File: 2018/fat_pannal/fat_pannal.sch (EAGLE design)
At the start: 31 parts, among them IC1 MEGA8-P, Q2 BUZ11BV, Q3 BUZ11BV, Q4 BUZ11BV, Q5 BUZ11BV, U1 TSR_1-2450

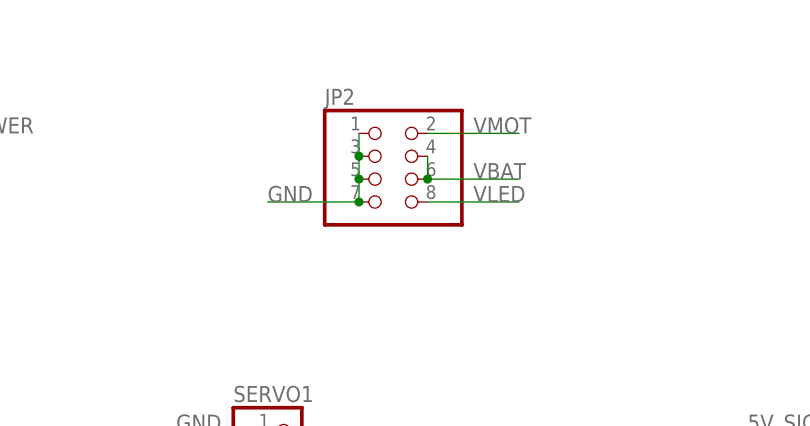
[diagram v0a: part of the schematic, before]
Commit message: [FAT pannal] Split cavalier in two.
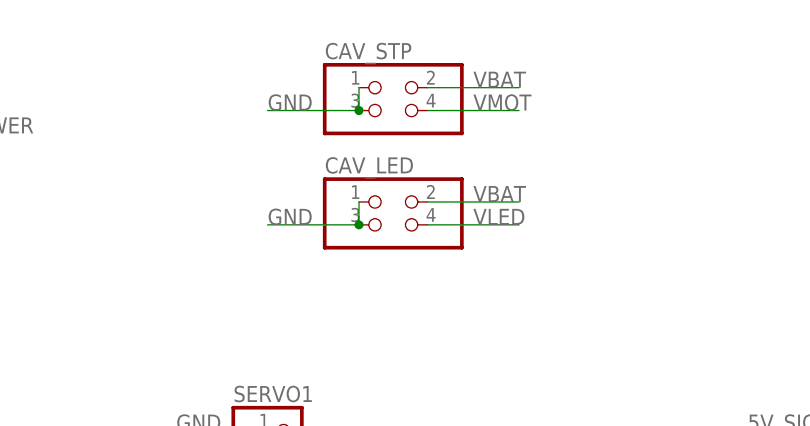
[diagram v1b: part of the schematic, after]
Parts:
- removed JP2: (no value), pinhead:PINHD-2X4
- added CAV_LED, CAV_STP: (no value), pinhead:PINHD-2X2
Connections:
- net GND: now also CAV_LED.1, CAV_LED.3, CAV_STP.1, CAV_STP.3; no longer JP2.1, JP2.3, JP2.5, JP2.7
- net VBAT: now also CAV_LED.2, CAV_STP.2; no longer JP2.4, JP2.6
- net VLED: now also CAV_LED.4; no longer JP2.8
- net VMOT: now also CAV_STP.4; no longer JP2.2
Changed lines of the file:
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@@
 <part name="SERVO3" library="pinhead" deviceset="PINHD-1X3" device=""/>
 <part name="REGU_5V_POWER" library="diy-modules" deviceset="DC-DC-STEP-DOWN-LM2596" device=""/>
-<part name="JP2" library="pinhead" deviceset="PINHD-2X4" device=""/>
 <part name="I2C" library="pinhead" deviceset="PINHD-1X4" device=""/>
 <part name="UART" library="pinhead" deviceset="PINHD-1X4" device=""/>
 <part name="X1" library="con-ptr500" deviceset="AK300/2" device=""/>
 <part name="U1" library="_traco_tsr-1" deviceset="TSR_1-*" device="" technology="2450"/>
+<part name="CAV_STP" library="pinhead" deviceset="PINHD-2X2" device=""/>
+<part name="CAV_LED" library="pinhead" deviceset="PINHD-2X2" device=""/>
 </parts>
 <sheets>
@@
 <instance part="SERVO3" gate="A" x="114.3" y="78.74"/>
 <instance part="REGU_5V_POWER" gate="G$1" x="53.34" y="134.62"/>
-<instance part="JP2" gate="A" x="124.46" y="134.62"/>
 <instance part="I2C" gate="A" x="180.34" y="83.82"/>
 <instance part="UART" gate="A" x="180.34" y="101.6"/>
@@
 <instance part="X1" gate="-2" x="5.08" y="134.62"/>
 <instance part="U1" gate="G$1" x="20.32" y="111.76"/>
+<instance part="CAV_STP" gate="A" x="127" y="142.24"/>
+<instance part="CAV_LED" gate="A" x="127" y="129.54"/>
 </instances>
 <busses>
@@
 </segment>
 <segment>
-<pinref part="JP2" gate="A" pin="1"/>
-<pinref part="JP2" gate="A" pin="3"/>
-<wire x1="121.92" y1="139.7" x2="121.92" y2="137.16" width="0.1524" layer="91"/>
-<pinref part="JP2" gate="A" pin="5"/>
-<wire x1="121.92" y1="137.16" x2="121.92" y2="134.62" width="0.1524" layer="91"/>
-<junction x="121.92" y="137.16"/>
-<pinref part="JP2" gate="A" pin="7"/>
-<wire x1="121.92" y1="134.62" x2="121.92" y2="132.08" width="0.1524" layer="91"/>
-<junction x="121.92" y="134.62"/>
-<wire x1="121.92" y1="132.08" x2="111.76" y2="132.08" width="0.1524" layer="91"/>
-<junction x="121.92" y="132.08"/>
-<label x="111.76" y="132.08" size="1.778" layer="95"/>
-</segment>
-<segment>
 <pinref part="STEPPER_DRIVER" gate="G$1" pin="GND2"/>
 <wire x1="114.3" y1="48.26" x2="121.92" y2="48.26" width="0.1524" layer="91"/>
@@
 <wire x1="20.32" y1="101.6" x2="25.4" y2="101.6" width="0.1524" layer="91"/>
 <label x="22.86" y="101.6" size="1.778" layer="95"/>
+</segment>
+<segment>
+<pinref part="CAV_LED" gate="A" pin="1"/>
+<pinref part="CAV_LED" gate="A" pin="3"/>
+<wire x1="121.92" y1="132.08" x2="121.92" y2="129.54" width="0.1524" layer="91"/>
+<wire x1="121.92" y1="129.54" x2="111.76" y2="129.54" width="0.1524" layer="91"/>
+<junction x="121.92" y="129.54"/>
+<label x="111.76" y="129.54" size="1.778" layer="95"/>
+</segment>
+<segment>
+<pinref part="CAV_STP" gate="A" pin="3"/>
+<wire x1="111.76" y1="142.24" x2="121.92" y2="142.24" width="0.1524" layer="91"/>
+<pinref part="CAV_STP" gate="A" pin="1"/>
+<wire x1="121.92" y1="142.24" x2="121.92" y2="144.78" width="0.1524" layer="91"/>
+<junction x="121.92" y="142.24"/>
+<label x="111.76" y="142.24" size="1.778" layer="95"/>
 </segment>
 </net>
@@
 </segment>
 <segment>
-<pinref part="JP2" gate="A" pin="8"/>
-<wire x1="129.54" y1="132.08" x2="139.7" y2="132.08" width="0.1524" layer="91"/>
-<label x="134.62" y="132.08" size="1.778" layer="95"/>
+<pinref part="CAV_LED" gate="A" pin="4"/>
+<wire x1="129.54" y1="129.54" x2="139.7" y2="129.54" width="0.1524" layer="91"/>
+<label x="134.62" y="129.54" size="1.778" layer="95"/>
 </segment>
 </net>
@@
 </segment>
 <segment>
-<pinref part="JP2" gate="A" pin="4"/>
-<pinref part="JP2" gate="A" pin="6"/>
-<wire x1="129.54" y1="137.16" x2="129.54" y2="134.62" width="0.1524" layer="91"/>
-<wire x1="129.54" y1="134.62" x2="139.7" y2="134.62" width="0.1524" layer="91"/>
-<junction x="129.54" y="134.62"/>
-<label x="134.62" y="134.62" size="1.778" layer="95"/>
-</segment>
-<segment>
 <pinref part="U1" gate="G$1" pin="VI"/>
 <wire x1="10.16" y1="111.76" x2="5.08" y2="111.76" width="0.1524" layer="91"/>
 <label x="2.54" y="111.76" size="1.778" layer="95"/>
 </segment>
+<segment>
+<pinref part="CAV_LED" gate="A" pin="2"/>
+<wire x1="129.54" y1="132.08" x2="139.7" y2="132.08" width="0.1524" layer="91"/>
+<label x="134.62" y="132.08" size="1.778" layer="95"/>
+</segment>
+<segment>
+<pinref part="CAV_STP" gate="A" pin="2"/>
+<wire x1="139.7" y1="144.78" x2="129.54" y2="144.78" width="0.1524" layer="91"/>
+<label x="134.62" y="144.78" size="1.778" layer="95"/>
+</segment>
 </net>
 <net name="VMOT" class="0">
-<segment>
-<pinref part="JP2" gate="A" pin="2"/>
-<wire x1="129.54" y1="139.7" x2="139.7" y2="139.7" width="0.1524" layer="91"/>
-<label x="134.62" y="139.7" size="1.778" layer="95"/>
-</segment>
 <segment>
 <pinref part="STEPPER_DRIVER" gate="G$1" pin="VMOT"/>
@@
 <label x="119.38" y="50.8" size="1.778" layer="95"/>
 </segment>
-</net>
+<segment>
+<pinref part="CAV_STP" gate="A" pin="4"/>
+<wire x1="129.54" y1="142.24" x2="139.7" y2="142.24" width="0.1524" layer="91"/>
+<label x="134.62" y="142.24" size="1.778" layer="95"/>
+</segment>
+</net>

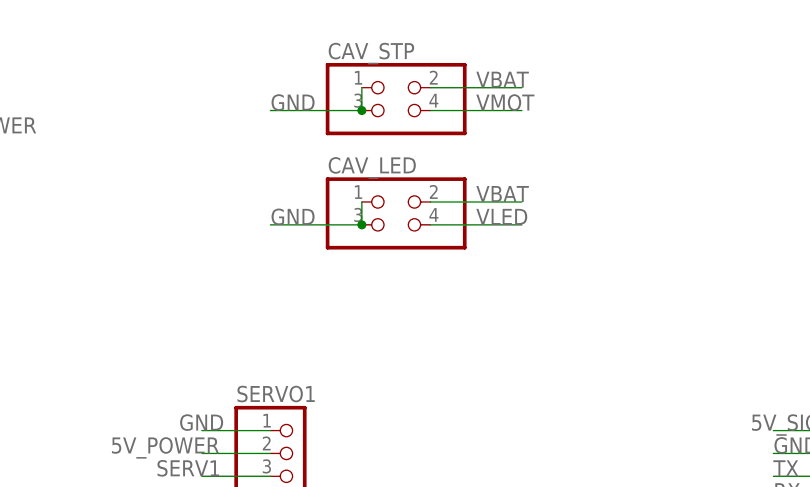
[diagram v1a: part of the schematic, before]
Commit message: [FAT pannal] Begins routing.
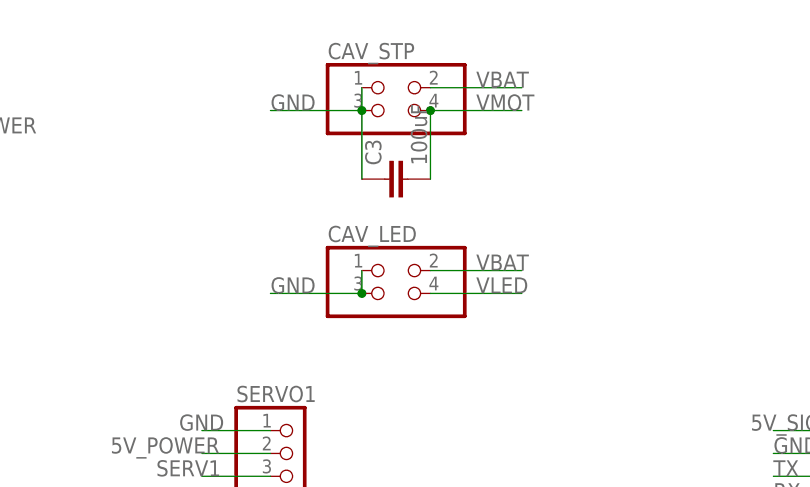
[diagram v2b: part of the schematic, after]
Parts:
- added C3: 100uF, rcl:C-EU025-050X050
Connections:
- net GND: now also C3.1
- net VMOT: now also C3.2
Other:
- moved on the sheet: CAV_LED
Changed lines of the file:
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@@
 <part name="CAV_STP" library="pinhead" deviceset="PINHD-2X2" device=""/>
 <part name="CAV_LED" library="pinhead" deviceset="PINHD-2X2" device=""/>
+<part name="C3" library="rcl" deviceset="C-EU" device="025-050X050" value="100uF"/>
 </parts>
 <sheets>
@@
 <instance part="U1" gate="G$1" x="20.32" y="111.76"/>
 <instance part="CAV_STP" gate="A" x="127" y="142.24"/>
-<instance part="CAV_LED" gate="A" x="127" y="129.54"/>
+<instance part="CAV_LED" gate="A" x="127" y="121.92"/>
+<instance part="C3" gate="G$1" x="124.46" y="134.62" rot="R90"/>
 </instances>
 <busses>
@@
 <pinref part="CAV_LED" gate="A" pin="1"/>
 <pinref part="CAV_LED" gate="A" pin="3"/>
-<wire x1="121.92" y1="132.08" x2="121.92" y2="129.54" width="0.1524" layer="91"/>
-<wire x1="121.92" y1="129.54" x2="111.76" y2="129.54" width="0.1524" layer="91"/>
-<junction x="121.92" y="129.54"/>
-<label x="111.76" y="129.54" size="1.778" layer="95"/>
+<wire x1="121.92" y1="124.46" x2="121.92" y2="121.92" width="0.1524" layer="91"/>
+<wire x1="121.92" y1="121.92" x2="111.76" y2="121.92" width="0.1524" layer="91"/>
+<junction x="121.92" y="121.92"/>
+<label x="111.76" y="121.92" size="1.778" layer="95"/>
 </segment>
 <segment>
@@
 <junction x="121.92" y="142.24"/>
 <label x="111.76" y="142.24" size="1.778" layer="95"/>
+<pinref part="C3" gate="G$1" pin="1"/>
+<wire x1="121.92" y1="134.62" x2="121.92" y2="142.24" width="0.1524" layer="91"/>
 </segment>
 </net>
@@
 <segment>
 <pinref part="CAV_LED" gate="A" pin="4"/>
-<wire x1="129.54" y1="129.54" x2="139.7" y2="129.54" width="0.1524" layer="91"/>
-<label x="134.62" y="129.54" size="1.778" layer="95"/>
+<wire x1="129.54" y1="121.92" x2="139.7" y2="121.92" width="0.1524" layer="91"/>
+<label x="134.62" y="121.92" size="1.778" layer="95"/>
 </segment>
 </net>
@@
 <segment>
 <pinref part="CAV_LED" gate="A" pin="2"/>
-<wire x1="129.54" y1="132.08" x2="139.7" y2="132.08" width="0.1524" layer="91"/>
-<label x="134.62" y="132.08" size="1.778" layer="95"/>
+<wire x1="129.54" y1="124.46" x2="139.7" y2="124.46" width="0.1524" layer="91"/>
+<label x="134.62" y="124.46" size="1.778" layer="95"/>
 </segment>
 <segment>
@@
 <wire x1="129.54" y1="142.24" x2="139.7" y2="142.24" width="0.1524" layer="91"/>
 <label x="134.62" y="142.24" size="1.778" layer="95"/>
-</segment>
-</net>
+<pinref part="C3" gate="G$1" pin="2"/>
+<wire x1="129.54" y1="134.62" x2="129.54" y2="142.24" width="0.1524" layer="91"/>
+<junction x="129.54" y="142.24"/>
+</segment>
+</net>

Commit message: [FAT pannal] Finish board V1.
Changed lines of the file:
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@@
 <pinref part="STEPPER_DRIVER" gate="G$1" pin="GND"/>
 <wire x1="114.3" y1="33.02" x2="124.46" y2="33.02" width="0.1524" layer="91"/>
+<label x="116.84" y="33.02" size="1.778" layer="95"/>
 </segment>
 <segment>
@@
 <pinref part="STEPPER_DRIVER" gate="G$1" pin="VDD"/>
 <wire x1="114.3" y1="35.56" x2="124.46" y2="35.56" width="0.1524" layer="91"/>
+<label x="116.84" y="35.56" size="1.778" layer="95"/>
 </segment>
 <segment>
